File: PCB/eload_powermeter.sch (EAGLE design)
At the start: 78 parts, among them IC1 ADS1115_IC, IC2 SGM8582, IC3 TP4056, IC4 FS312F-G, IC5 MT3608, IC6 FS8205, K2 TXD2SA-4.5V, Q1 BSS123, Q3 BSS123, Q4 IRF520, Q5 BSS123, Q6 IRF520, Q7 IRF520, U1 ATMEGA328P, Y1 16MHz

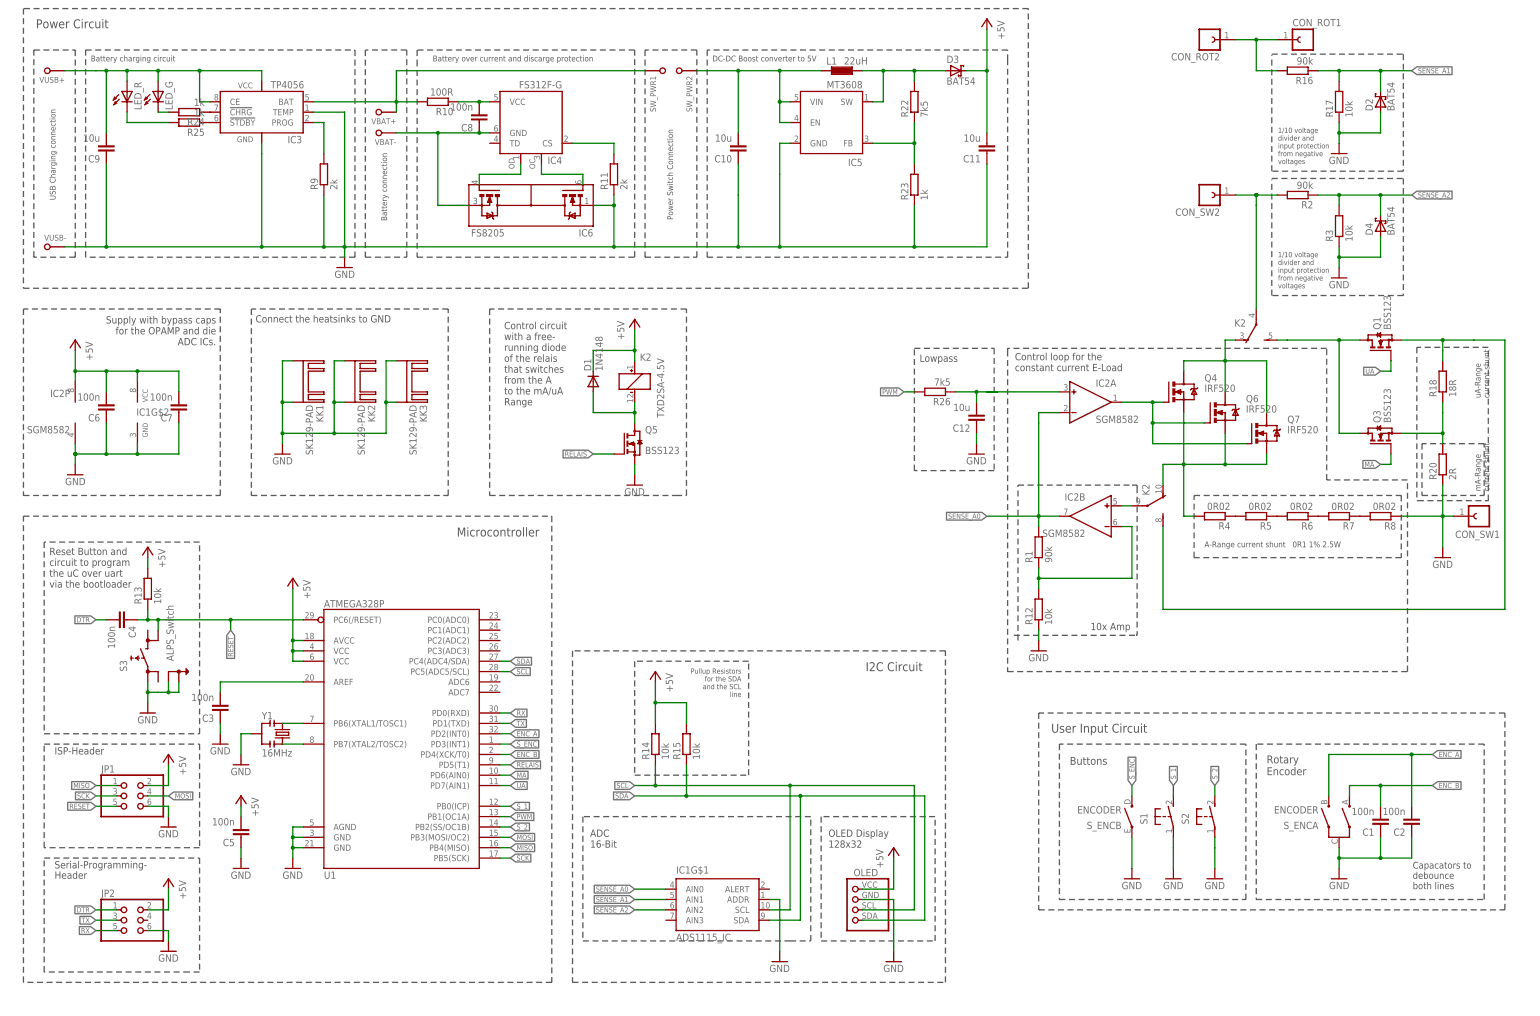
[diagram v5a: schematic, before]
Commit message: Adding Battery measurement and power on led. Cleaning up silk screen.
Connecting both terminals of the battery  to adc pins of the uC to measure the battery capacity. Adding the connections of the power-on led that is build in to the button.
Cleaning up the component names of the silk screen.
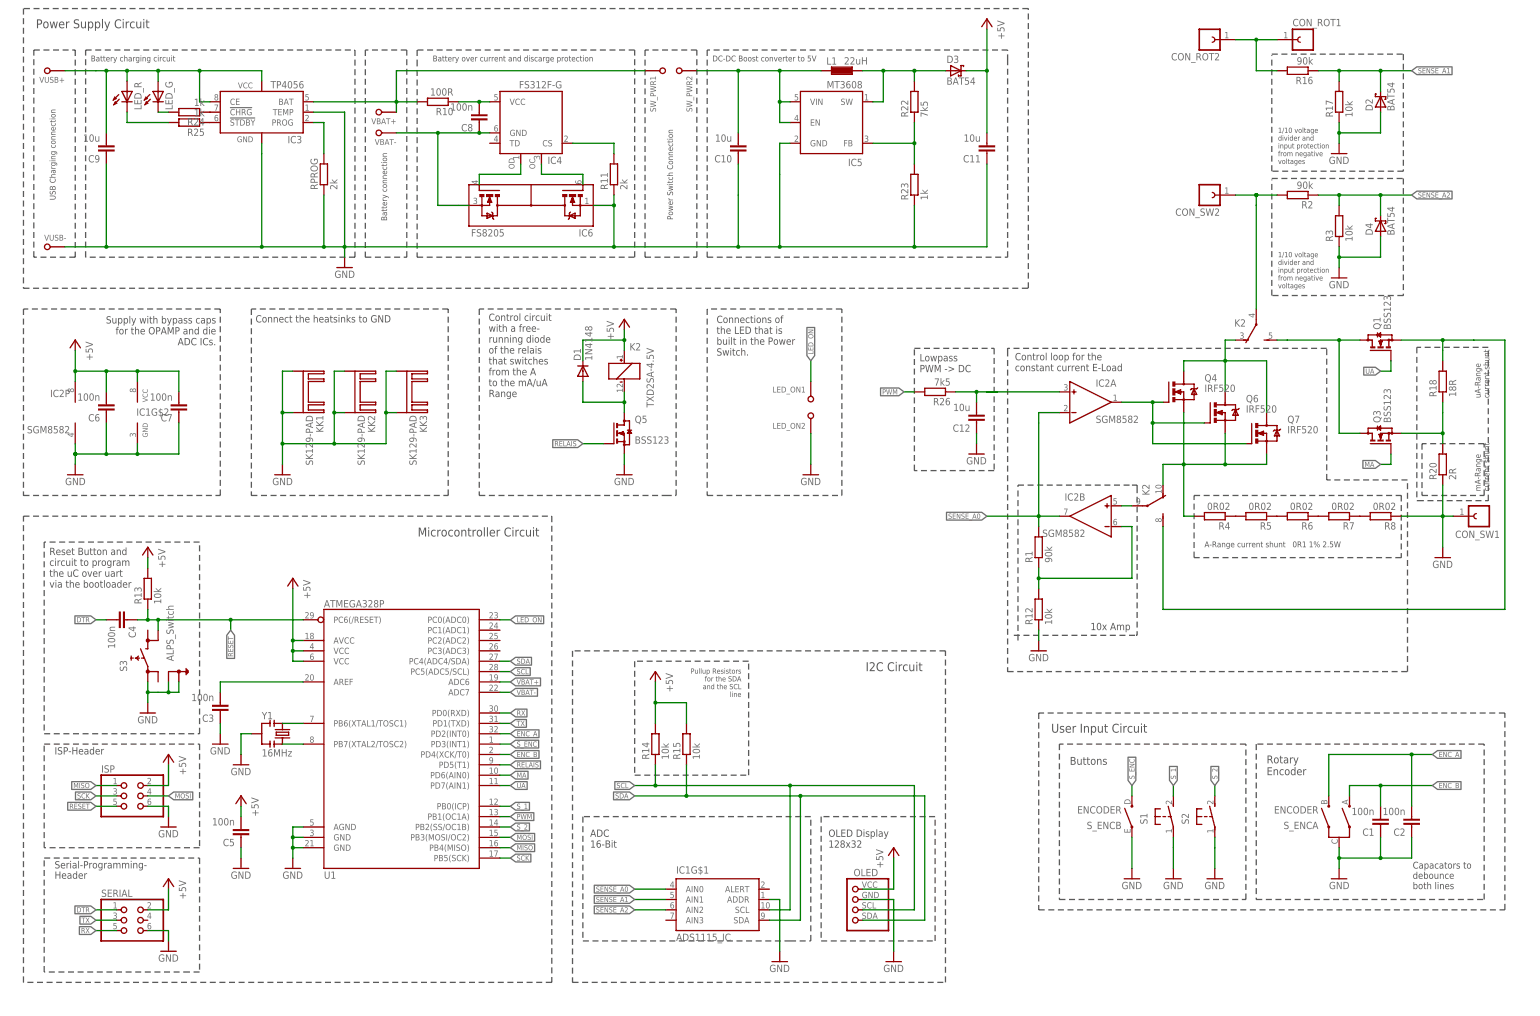
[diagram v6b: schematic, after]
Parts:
- added LED_ON1, LED_ON2: SOLDER_PAD, eload_powermeter:SOLDER_PAD
- renumbered JP1 to ISP, JP2 to SERIAL, R9 to RPROG
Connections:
- new net LED_ON: LED_ON1.P$1, U1.PC0(ADC0)
- net GND: now also LED_ON2.P$1
- net VBAT+: now also U1.ADC6
- net VBAT-: now also U1.ADC7
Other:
- note added: "Connections of the LED that is built in the Power Switch."
- note added: "Lowpass PWM -> DC"
- note added: "Microcontroller Circuit"
- note added: "Power Supply Circuit"
- note removed: "Lowpass"
- note removed: "Microcontroller"
- note removed: "Power Circuit"
- moved on the sheet: D1, K2, KK1, KK2, KK3, Q5
